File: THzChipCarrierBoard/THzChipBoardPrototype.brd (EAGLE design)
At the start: 34.3 x 27.9 mm, 8 parts

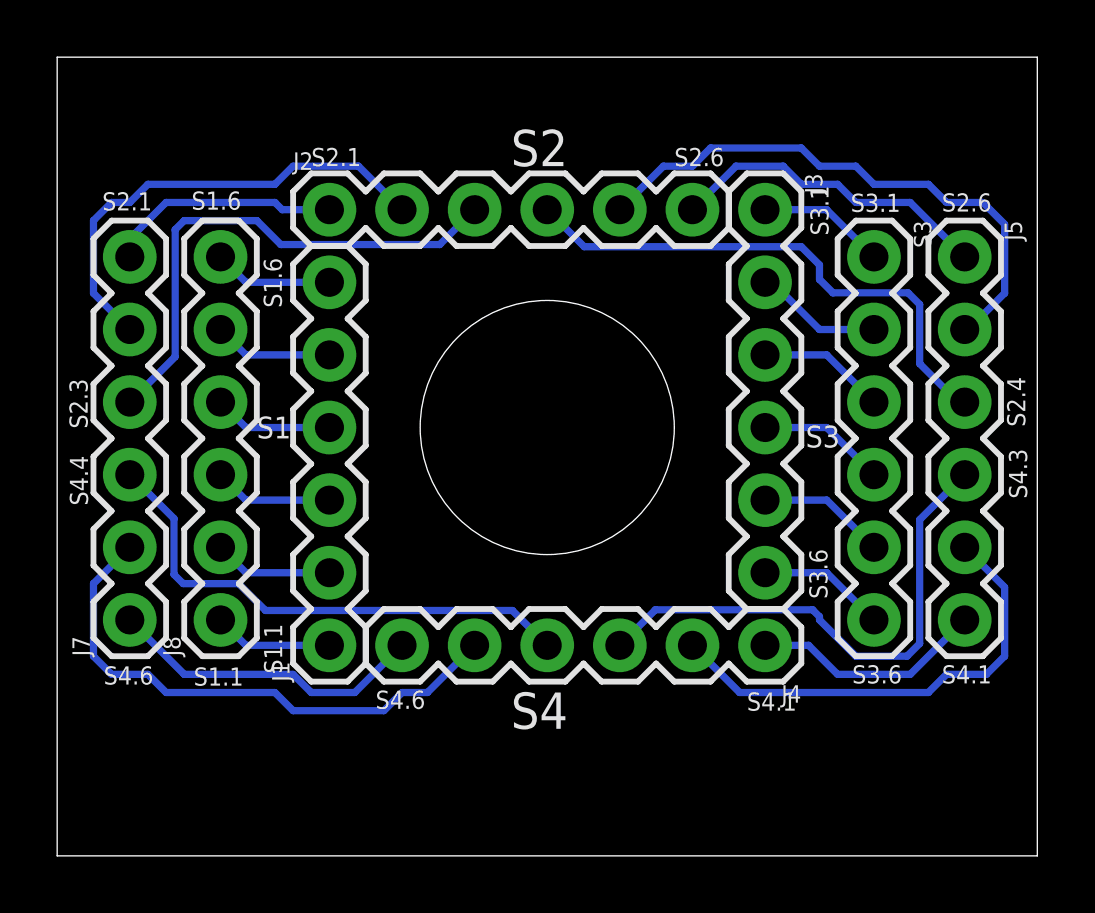
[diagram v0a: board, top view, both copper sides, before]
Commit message: Updated ChipCarrier board design, added copper plate backing, soldermasks and what not
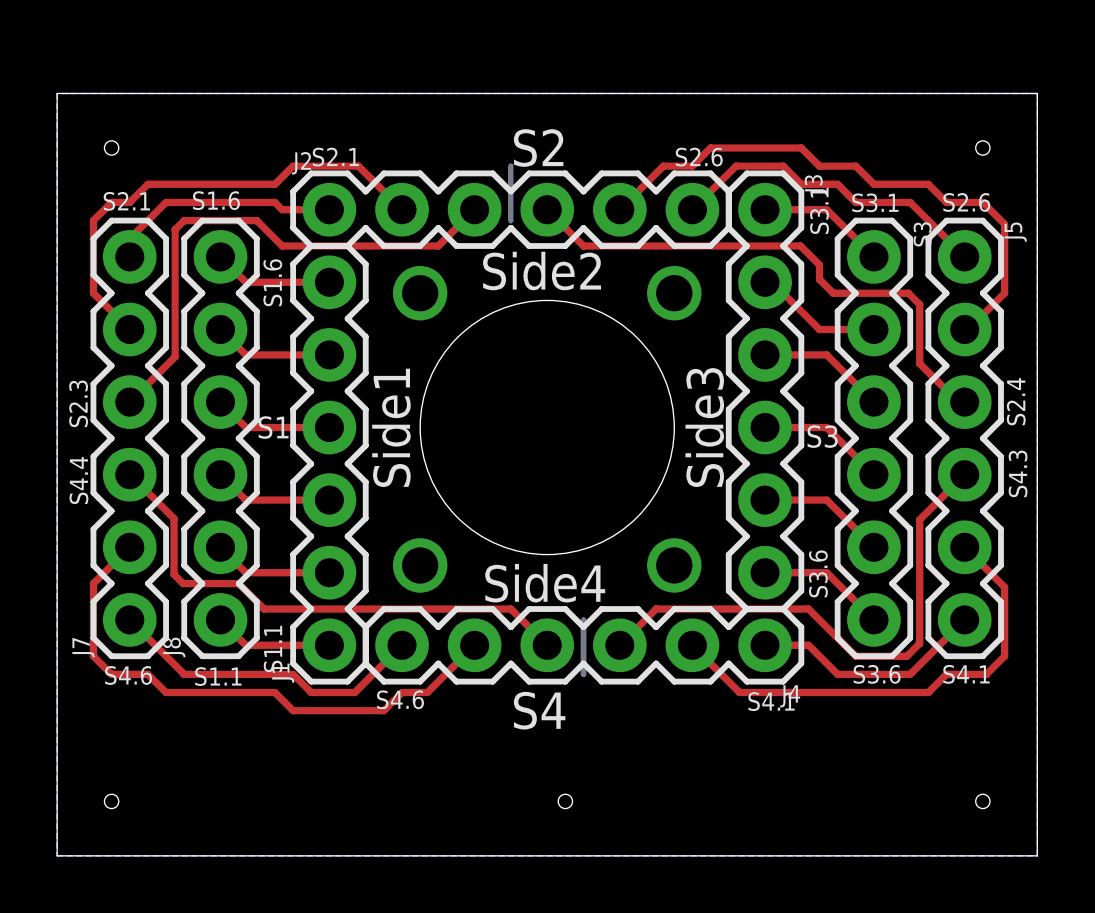
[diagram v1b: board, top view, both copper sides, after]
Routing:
- net GND: track 0.00 -> 3.81 mm, vias 0 -> 4
- added copper zone on layer 16, net GND
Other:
- board size 34.3 x 27.9 mm -> 34.3 x 26.7 mm
- board text added: "Side1"
- board text added: "Side2"
- board text added: "Side3"
- board text added: "Side4"
